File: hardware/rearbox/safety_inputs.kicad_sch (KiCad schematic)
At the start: 13 parts, among them U9 TCA6416ARTWR

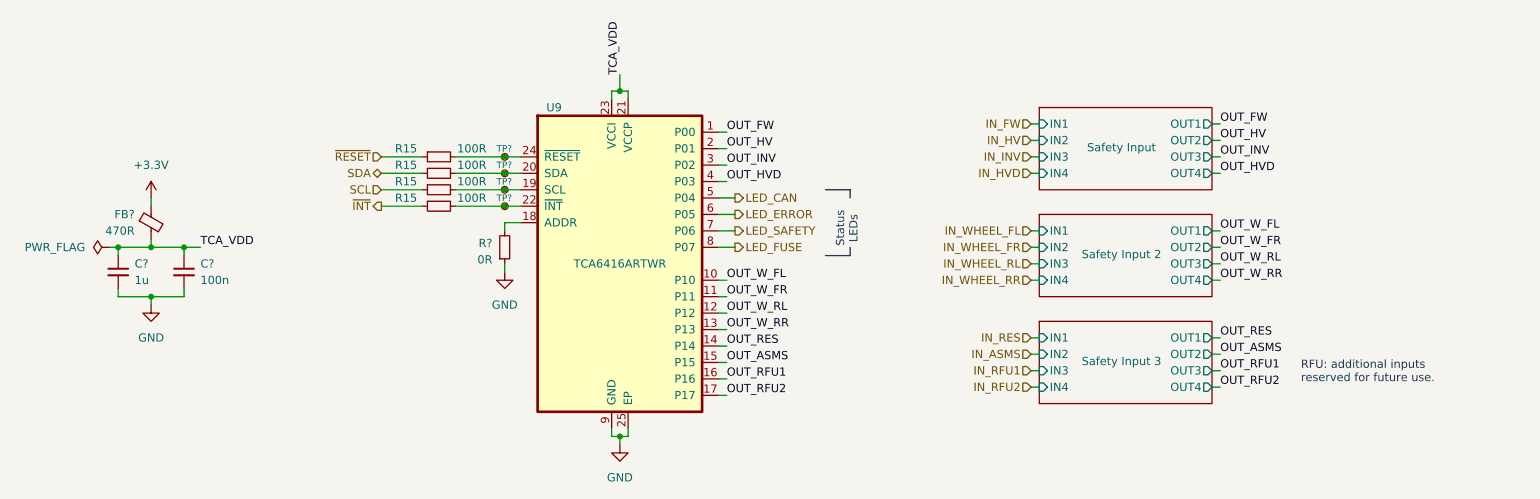
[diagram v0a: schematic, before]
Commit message: Place components on the PCB
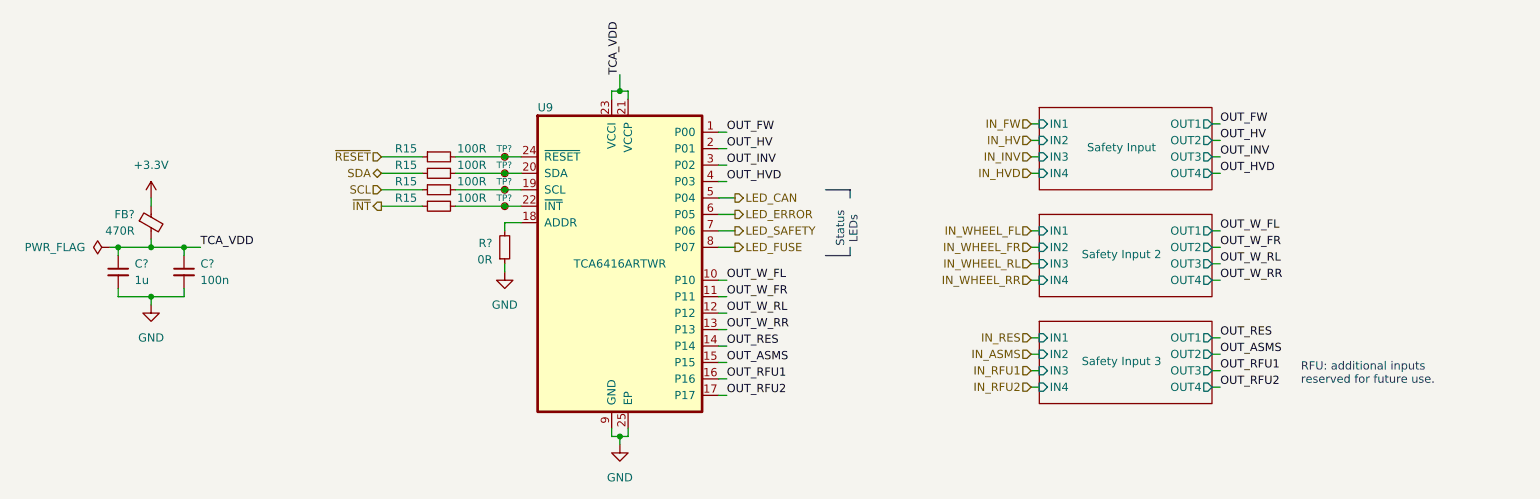
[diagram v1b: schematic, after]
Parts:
- U9: footprint QFN50P400X400X80-25N -> Local_Library:QFN50P400X400X80-25N
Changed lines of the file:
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@@
   (title_block
     (title "Safety Inputs")
-    (date "2023-10-01")
+    (date "2023-11-02")
     (rev "${REVISION}")
     (company "Author: I. Kajdan")
@@
     (stroke (width -0.0001) (type default))
     (fill (type none))
-    (effects (font (size 1.27 1.27)) (justify left))
+    (effects (font (size 1.27 1.27)) (justify left top))
   )
   (text "Status\n LEDs\n" (at 175.26 96.52 90)
@@
         )
         (path "/b652b05a-4e3d-4ad1-b032-18886abe7d45/5d9671f9-6e77-4376-b4d6-afe9f66a07c2"
-          (reference "#PWR0111") (unit 1)
+          (reference "#PWR0108") (unit 1)
         )
       )
@@
         )
         (path "/b652b05a-4e3d-4ad1-b032-18886abe7d45/5d9671f9-6e77-4376-b4d6-afe9f66a07c2"
-          (reference "R68") (unit 1)
+          (reference "R42") (unit 1)
         )
       )
@@
         )
         (path "/b652b05a-4e3d-4ad1-b032-18886abe7d45/5d9671f9-6e77-4376-b4d6-afe9f66a07c2"
-          (reference "#PWR0110") (unit 1)
+          (reference "#PWR0107") (unit 1)
         )
       )
@@
         )
         (path "/b652b05a-4e3d-4ad1-b032-18886abe7d45/5d9671f9-6e77-4376-b4d6-afe9f66a07c2"
-          (reference "R70") (unit 1)
+          (reference "R44") (unit 1)
         )
       )
@@
         )
         (path "/b652b05a-4e3d-4ad1-b032-18886abe7d45/5d9671f9-6e77-4376-b4d6-afe9f66a07c2"
-          (reference "TP27") (unit 1)
+          (reference "TP24") (unit 1)
         )
       )
@@
         )
         (path "/b652b05a-4e3d-4ad1-b032-18886abe7d45/5d9671f9-6e77-4376-b4d6-afe9f66a07c2"
-          (reference "R69") (unit 1)
+          (reference "R43") (unit 1)
         )
       )
@@
         )
         (path "/b652b05a-4e3d-4ad1-b032-18886abe7d45/5d9671f9-6e77-4376-b4d6-afe9f66a07c2"
-          (reference "#PWR0109") (unit 1)
+          (reference "#PWR0106") (unit 1)
         )
       )
@@
         )
         (path "/b652b05a-4e3d-4ad1-b032-18886abe7d45/5d9671f9-6e77-4376-b4d6-afe9f66a07c2"
-          (reference "R72") (unit 1)
+          (reference "R46") (unit 1)
         )
       )
@@
         )
         (path "/b652b05a-4e3d-4ad1-b032-18886abe7d45/5d9671f9-6e77-4376-b4d6-afe9f66a07c2"
-          (reference "#PWR0108") (unit 1)
+          (reference "#PWR0105") (unit 1)
         )
       )
@@
         )
         (path "/b652b05a-4e3d-4ad1-b032-18886abe7d45/5d9671f9-6e77-4376-b4d6-afe9f66a07c2"
-          (reference "R71") (unit 1)
+          (reference "R45") (unit 1)
         )
       )
@@
         )
         (path "/b652b05a-4e3d-4ad1-b032-18886abe7d45/5d9671f9-6e77-4376-b4d6-afe9f66a07c2"
-          (reference "C36") (unit 1)
+          (reference "C35") (unit 1)
         )
       )
@@
         )
         (path "/b652b05a-4e3d-4ad1-b032-18886abe7d45/5d9671f9-6e77-4376-b4d6-afe9f66a07c2"
-          (reference "C35") (unit 1)
+          (reference "C34") (unit 1)
         )
       )
@@
         )
         (path "/b652b05a-4e3d-4ad1-b032-18886abe7d45/5d9671f9-6e77-4376-b4d6-afe9f66a07c2"
-          (reference "TP30") (unit 1)
+          (reference "TP27") (unit 1)
         )
       )
@@
         )
         (path "/b652b05a-4e3d-4ad1-b032-18886abe7d45/5d9671f9-6e77-4376-b4d6-afe9f66a07c2"
-          (reference "TP29") (unit 1)
+          (reference "TP26") (unit 1)
         )
       )
@@
   (symbol (lib_id "TCA6416ARTWR:TCA6416ARTWR") (at 138.43 99.06 0) (unit 1)
     (in_bom yes) (on_board yes) (dnp no)
-    (property "Reference" "U9" (at 128.27 74.93 0)
-      (effects (font (size 1.27 1.27)))
+    (property "Reference" "U9" (at 125.73 74.93 0)
+      (effects (font (size 1.27 1.27)) (justify left))
     )
     (property "Value" "TCA6416ARTWR" (at 138.43 99.06 0)
       (effects (font (size 1.27 1.27)))
     )
-    (property "Footprint" "QFN50P400X400X80-25N" (at 138.43 99.06 0)
+    (property "Footprint" "Local_Library:QFN50P400X400X80-25N" (at 138.43 99.06 0)
       (effects (font (size 1.27 1.27)) (justify bottom) hide)
     )
@@
         )
         (path "/b652b05a-4e3d-4ad1-b032-18886abe7d45/5d9671f9-6e77-4376-b4d6-afe9f66a07c2"
-          (reference "TP28") (unit 1)
-        )
-      )
+          (reference "TP25") (unit 1)
+        )
+      )

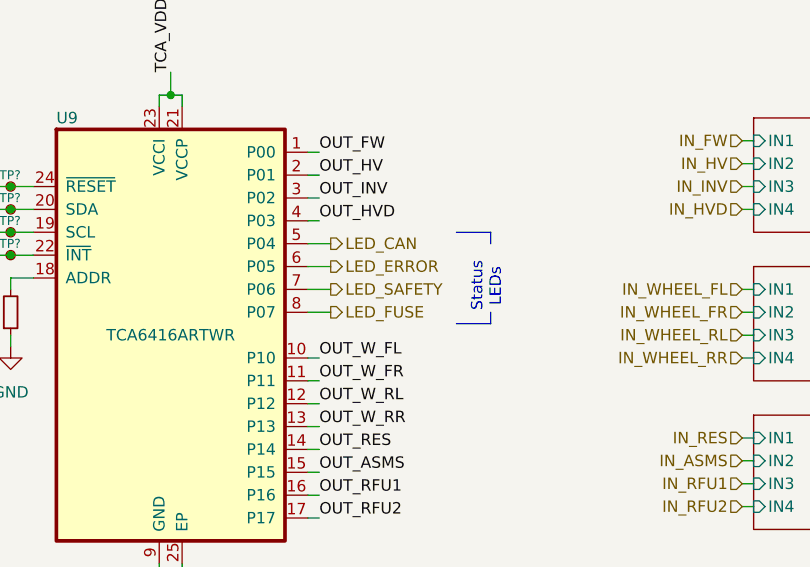
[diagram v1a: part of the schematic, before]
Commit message: Align footprint references
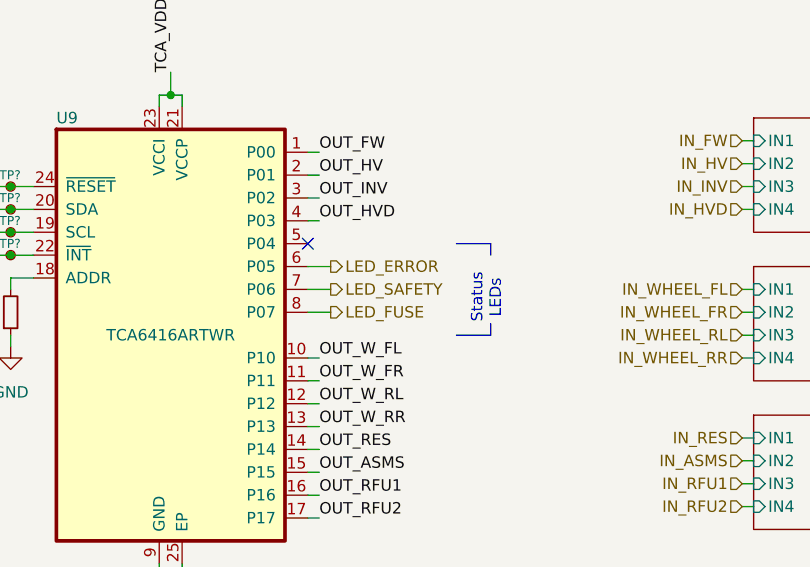
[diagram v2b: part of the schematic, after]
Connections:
- net LED_CAN: no longer names the net of U9.5 (P04)
- no-connect marks 0 -> 1
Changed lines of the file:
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@@
   (junction (at 138.43 72.39) (diameter 0) (color 0 0 0 0)
   )
+  (no_connect (at 153.67 88.9))
   (wire (pts (xy 154.94 101.6) (xy 153.67 101.6))
     (stroke (width 0) (type default))
@@
     (stroke (width 0) (type default))
   )
-  (polyline (pts (xy 170.18 97.79) (xy 173.99 97.79))
-    (stroke (width 0) (type default))
-  )
-  (polyline (pts (xy 173.99 96.52) (xy 173.99 97.79))
+  (polyline (pts (xy 170.18 99.06) (xy 173.99 99.06))
+    (stroke (width 0) (type default))
+  )
+  (polyline (pts (xy 173.99 97.79) (xy 173.99 99.06))
     (stroke (width 0) (type default))
   )
@@
     (stroke (width 0) (type default))
   )
-  (wire (pts (xy 153.67 88.9) (xy 156.21 88.9))
-    (stroke (width 0) (type default))
-  )
   (wire (pts (xy 60.96 104.14) (xy 60.96 102.87))
     (stroke (width 0) (type default))
   )
-  (polyline (pts (xy 173.99 87.63) (xy 173.99 88.9))
+  (polyline (pts (xy 173.99 88.9) (xy 173.99 90.17))
     (stroke (width 0) (type default))
   )
@@
     (stroke (width 0) (type default))
   )
-  (polyline (pts (xy 170.18 87.63) (xy 173.99 87.63))
+  (polyline (pts (xy 170.18 88.9) (xy 173.99 88.9))
     (stroke (width 0) (type default))
   )
@@
     (effects (font (size 1.27 1.27)) (justify left top))
   )
-  (text "Status\n LEDs\n" (at 175.26 96.52 90)
+  (text "Status\n LEDs\n" (at 175.26 97.79 90)
     (effects (font (size 1.27 1.27)) (justify left bottom))
   )
@@
     (effects (font (size 1.27 1.27)) (justify right))
   )
-  (hierarchical_label "LED_CAN" (shape output) (at 156.21 88.9 0) (fields_autoplaced)
-    (effects (font (size 1.27 1.27)) (justify left))
-  )
   (hierarchical_label "IN_WHEEL_RR" (shape input) (at 201.93 101.6 180) (fields_autoplaced)
     (effects (font (size 1.27 1.27)) (justify right))
@@
         )
         (path "/b652b05a-4e3d-4ad1-b032-18886abe7d45/5d9671f9-6e77-4376-b4d6-afe9f66a07c2"
-          (reference "#PWR0108") (unit 1)
+          (reference "#PWR0109") (unit 1)
         )
       )
@@
         )
         (path "/b652b05a-4e3d-4ad1-b032-18886abe7d45/5d9671f9-6e77-4376-b4d6-afe9f66a07c2"
-          (reference "R42") (unit 1)
+          (reference "R41") (unit 1)
         )
       )
@@
         )
         (path "/b652b05a-4e3d-4ad1-b032-18886abe7d45/5d9671f9-6e77-4376-b4d6-afe9f66a07c2"
-          (reference "#PWR0107") (unit 1)
+          (reference "#PWR0108") (unit 1)
         )
       )
@@
         )
         (path "/b652b05a-4e3d-4ad1-b032-18886abe7d45/5d9671f9-6e77-4376-b4d6-afe9f66a07c2"
-          (reference "R44") (unit 1)
+          (reference "R43") (unit 1)
         )
       )
@@
         )
         (path "/b652b05a-4e3d-4ad1-b032-18886abe7d45/5d9671f9-6e77-4376-b4d6-afe9f66a07c2"
-          (reference "R43") (unit 1)
+          (reference "R42") (unit 1)
         )
       )
@@
         )
         (path "/b652b05a-4e3d-4ad1-b032-18886abe7d45/5d9671f9-6e77-4376-b4d6-afe9f66a07c2"
-          (reference "#PWR0106") (unit 1)
+          (reference "#PWR0107") (unit 1)
         )
       )
@@
         )
         (path "/b652b05a-4e3d-4ad1-b032-18886abe7d45/5d9671f9-6e77-4376-b4d6-afe9f66a07c2"
-          (reference "R46") (unit 1)
+          (reference "R45") (unit 1)
         )
       )
@@
         )
         (path "/b652b05a-4e3d-4ad1-b032-18886abe7d45/5d9671f9-6e77-4376-b4d6-afe9f66a07c2"
-          (reference "#PWR0105") (unit 1)
+          (reference "#PWR0106") (unit 1)
         )
       )
@@
         )
         (path "/b652b05a-4e3d-4ad1-b032-18886abe7d45/5d9671f9-6e77-4376-b4d6-afe9f66a07c2"
-          (reference "R45") (unit 1)
-        )
-      )
+          (reference "R44") (unit 1)
+        )
+      )

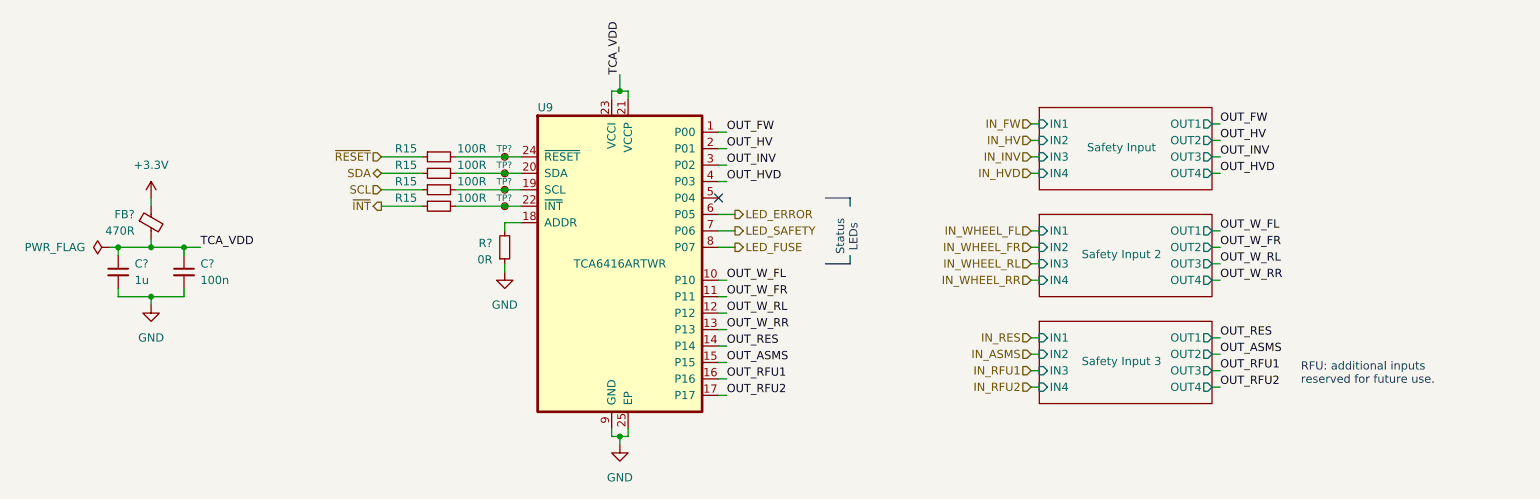
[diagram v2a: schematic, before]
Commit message: Route PCB tracks
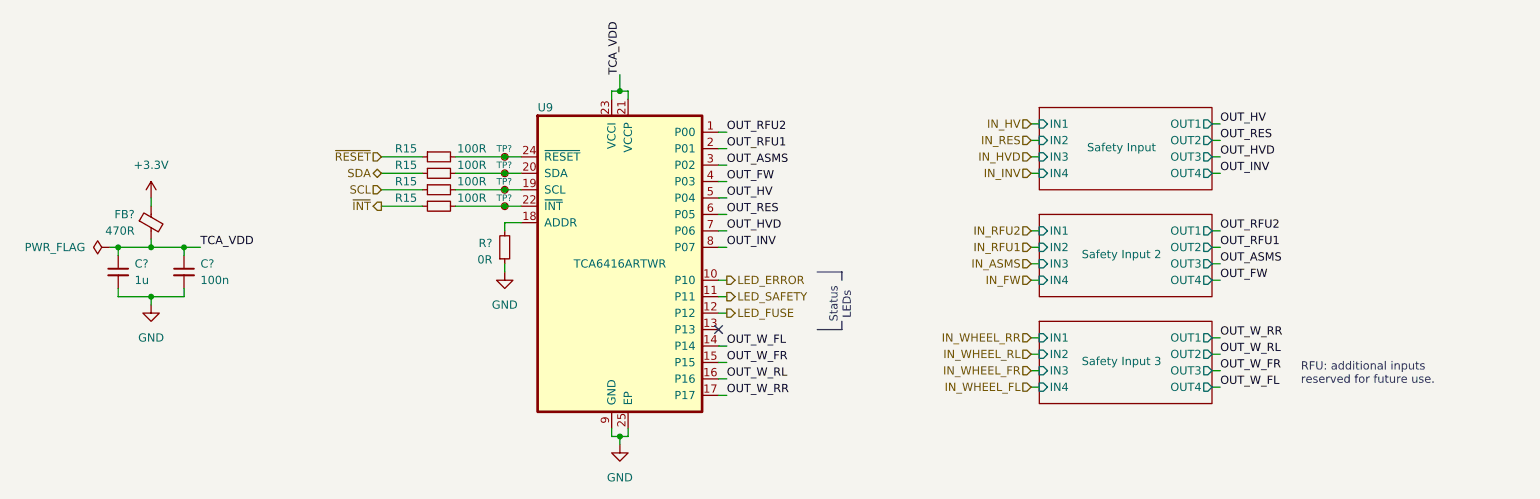
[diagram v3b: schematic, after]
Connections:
- net LED_ERROR: now also U9.10 (P10); no longer U9.6 (P05)
- net LED_FUSE: now also U9.12 (P12); no longer U9.8 (P07)
- net LED_SAFETY: now also U9.11 (P11); no longer U9.7 (P06)
- net OUT_ASMS: now also U9.3 (P02); no longer U9.15 (P15)
- net OUT_FW: now also U9.4 (P03); no longer U9.1 (P00)
- net OUT_HV: now also U9.5 (P04); no longer U9.2 (P01)
- net OUT_HVD: now also U9.7 (P06); no longer U9.4 (P03)
- net OUT_INV: now also U9.8 (P07); no longer U9.3 (P02)
- net OUT_RES: now also U9.6 (P05); no longer U9.14 (P14)
- net OUT_RFU1: now also U9.2 (P01); no longer U9.16 (P16)
- net OUT_RFU2: now also U9.1 (P00); no longer U9.17 (P17)
- net OUT_W_FL: now also U9.14 (P14); no longer U9.10 (P10)
- net OUT_W_FR: now also U9.15 (P15); no longer U9.11 (P11)
- net OUT_W_RL: now also U9.16 (P16); no longer U9.12 (P12)
- net OUT_W_RR: now also U9.17 (P17); no longer U9.13 (P13)

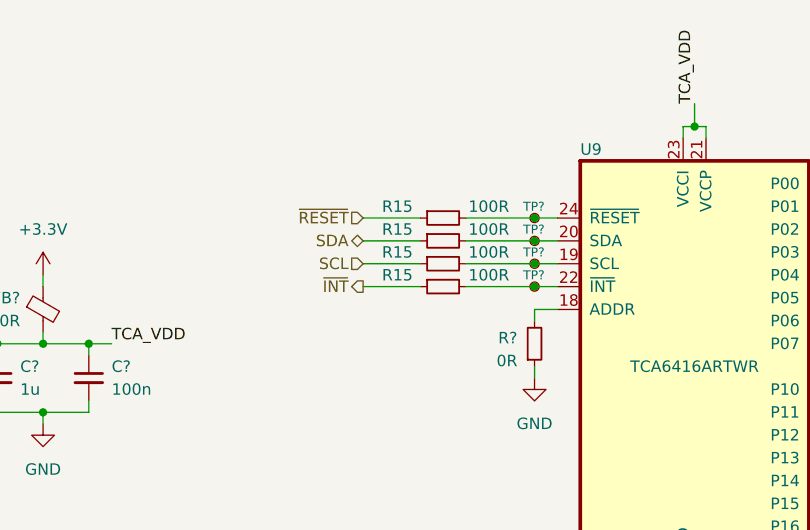
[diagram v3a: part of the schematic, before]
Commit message: Fix DRCs
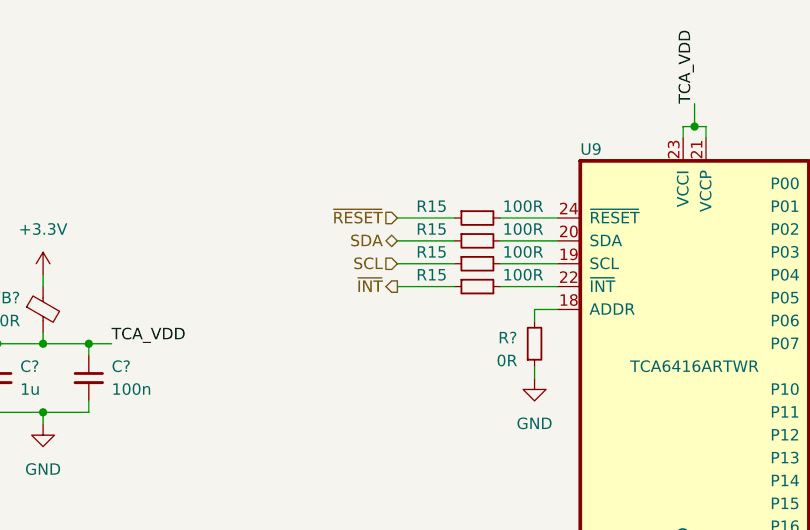
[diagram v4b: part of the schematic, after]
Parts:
- removed TP? (x4): TestPoint_Small, TestPoint:TestPoint_Pad_D1.0mm, symbol Connector:TestPoint_Small
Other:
- moved on the sheet: R15

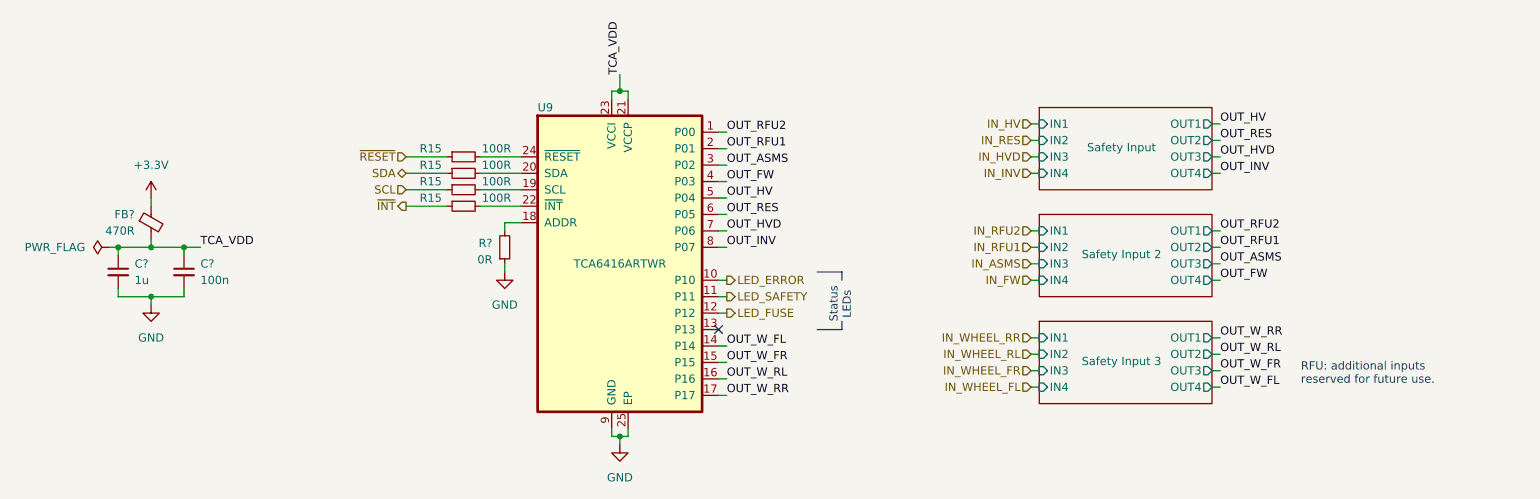
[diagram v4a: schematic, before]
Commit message: Route the tracks on the connector PCB
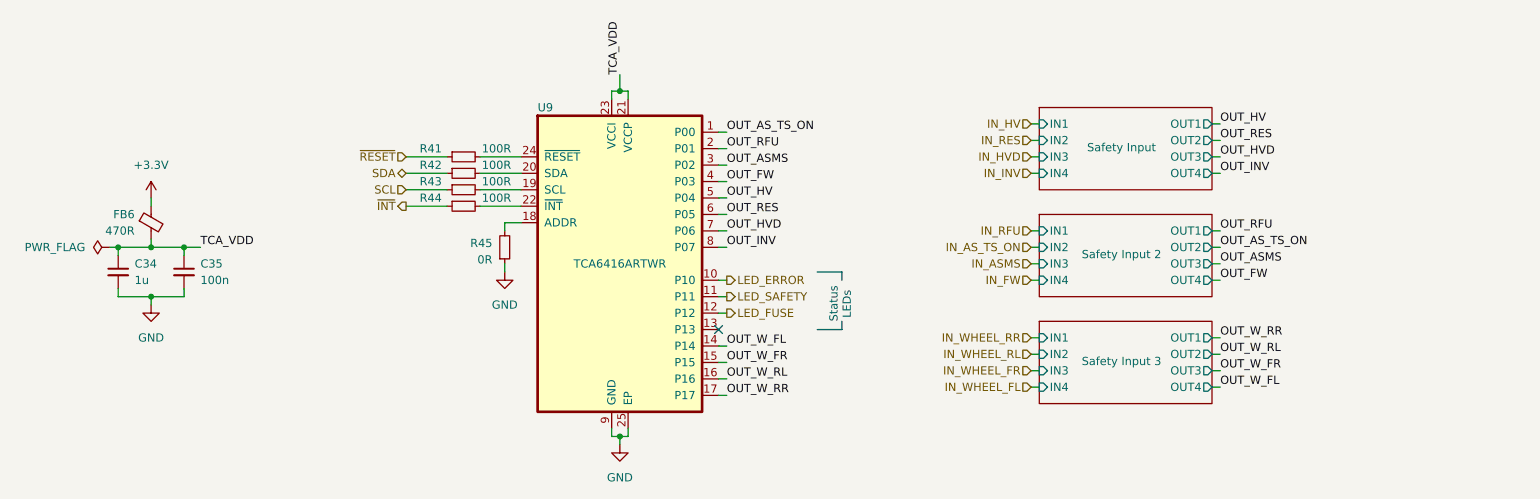
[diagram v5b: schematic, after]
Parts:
- gave numbers to parts that had none: 4
- renumbered R15 to R41, R15 to R42, R15 to R43, R15 to R44
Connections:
- net OUT_RFU1 renamed OUT_RFU
- net OUT_RFU2 renamed OUT_AS_TS_ON
